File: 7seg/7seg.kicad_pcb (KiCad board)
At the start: 2 copper layers, 93.9 x 27.9 mm, 13 parts, among them J1 9pin_header, U1 LTS-4031JR, U2 LTS-4031JR, U3 LTS-4031JR, U4 LTS-4031JR, U5 LTS-4031JR, U6 LTS-4031JR, U7 LTS-4031JR, U8 LTS-4031JR

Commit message: more library changes
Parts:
- H1, H2, H3, H4: footprint MountingHole:MountingHole_2.2mm_M2_Pad -> footprints:MountingHole_2.2mm_M2_Pad
- J1: footprint SamacSys_Parts:HDRV9W63P0X254_1X9_2286X369X950P -> footprints:header
- U1, U2, U3, U4, U5, U6, U7, U8: footprint SamacSys_Parts:DIPS762W50P254L1290H725Q10N -> footprints:7seg

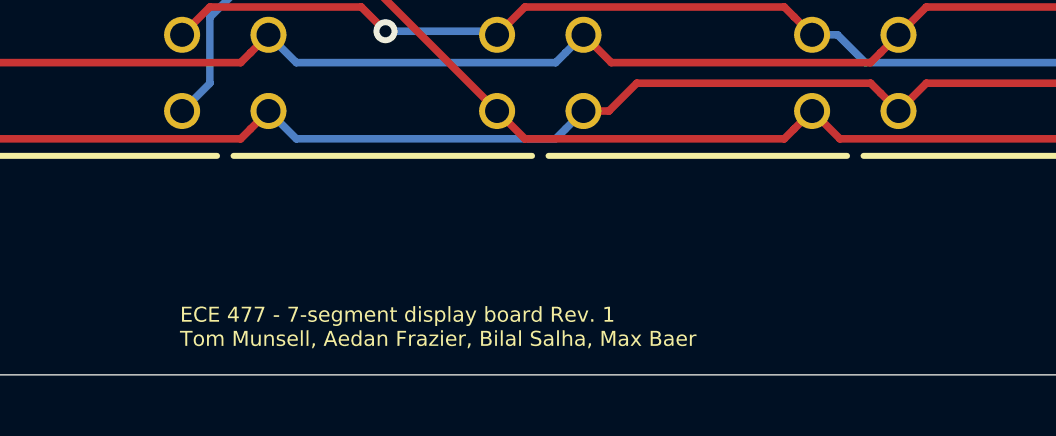
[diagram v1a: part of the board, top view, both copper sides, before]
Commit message: cleaned up directories, silkscreen
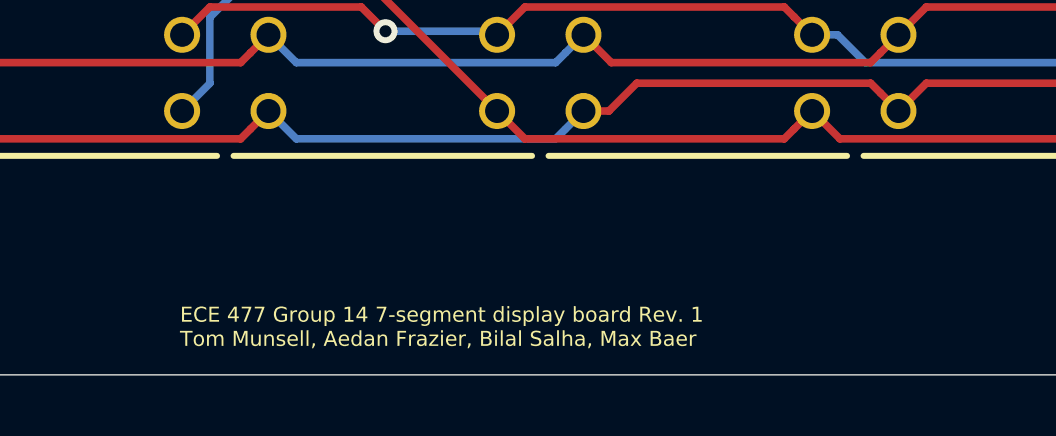
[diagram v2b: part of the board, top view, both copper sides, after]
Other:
- board text added: "ECE 477 Group 14 7-segment display board Rev. 1 Tom Munsell, Aedan Frazier, Bilal Salha, Max Baer"
- board text removed: "ECE 477 - 7-segment display board Rev. 1 Tom Munsell, Aedan Frazier, Bilal Salha, Max Baer"
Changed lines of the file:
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@@
       (net 7 "Net-(J1-Pad3)"))
   )
-  (gr_text "ECE 477 - 7-segment display board Rev. 1\nTom Munsell, Aedan Frazier, Bilal Salha, Max Baer" (at 82.55 92.3544) (layer F.SilkS)
+  (gr_text "ECE 477 Group 14 7-segment display board Rev. 1\nTom Munsell, Aedan Frazier, Bilal Salha, Max Baer" (at 82.55 92.3544) (layer F.SilkS)
     (effects (font (size 0.5 0.5) (thickness 0.125)) (justify left))
   )

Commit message: Added reset button, fixed 7seg pin order
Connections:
- net Net-(J1-Pad7) renamed /DIG6
- J1 pad 1: Net-(J1-Pad1) -> /DIG3
- J1 pad 2: Net-(J1-Pad2) -> /DIG2
- J1 pad 3: Net-(J1-Pad3) -> /DIG1
- J1 pad 4: Net-(J1-Pad4) -> /DIG0
- J1 pad 5: Net-(J1-Pad5) -> /a
- J1 pad 6: Net-(J1-Pad6) -> /DIG7
- J1 pad 8: Net-(J1-Pad8) -> /DIG5
- J1 pad 9: Net-(J1-Pad9) -> /DIG4
- U1 pad 1: Net-(J1-Pad3) -> /DIG2
- U1 pad 10: Net-(J1-Pad9) -> /a
- U1 pad 2: Net-(J1-Pad4) -> /DIG3
- U1 pad 3: Net-(J1-Pad1) -> /DIG0
- U1 pad 4: Net-(J1-Pad5) -> /DIG4
- U1 pad 5: Net-(J1-Pad6) -> /DIG5
- U1 pad 6: Net-(J1-Pad2) -> /DIG1
- U1 pad 8: Net-(J1-Pad1) -> /DIG0
- U1 pad 9: Net-(J1-Pad8) -> /DIG7
- U2 pad 1: Net-(J1-Pad3) -> /DIG2
- U2 pad 10: Net-(J1-Pad9) -> /a
- U2 pad 2: Net-(J1-Pad4) -> /DIG3
- U2 pad 3: Net-(J1-Pad2) -> /DIG1
- U2 pad 4: Net-(J1-Pad5) -> /DIG4
- U2 pad 5: Net-(J1-Pad6) -> /DIG5
- U2 pad 6: Net-(J1-Pad1) -> /DIG0
- U2 pad 8: Net-(J1-Pad2) -> /DIG1
- U2 pad 9: Net-(J1-Pad8) -> /DIG7
- U3 pad 1: Net-(J1-Pad2) -> /DIG1
- U3 pad 10: Net-(J1-Pad9) -> /a
- U3 pad 2: Net-(J1-Pad4) -> /DIG3
- U3 pad 3: Net-(J1-Pad3) -> /DIG2
- U3 pad 4: Net-(J1-Pad5) -> /DIG4
- U3 pad 5: Net-(J1-Pad6) -> /DIG5
- U3 pad 6: Net-(J1-Pad1) -> /DIG0
- U3 pad 8: Net-(J1-Pad3) -> /DIG2
- U3 pad 9: Net-(J1-Pad8) -> /DIG7
- U4 pad 1: Net-(J1-Pad2) -> /DIG1
- U4 pad 10: Net-(J1-Pad9) -> /a
- U4 pad 2: Net-(J1-Pad3) -> /DIG2
- U4 pad 3: Net-(J1-Pad4) -> /DIG3
- U4 pad 4: Net-(J1-Pad5) -> /DIG4
- U4 pad 5: Net-(J1-Pad6) -> /DIG5
- U4 pad 6: Net-(J1-Pad1) -> /DIG0
- U4 pad 8: Net-(J1-Pad4) -> /DIG3
- U4 pad 9: Net-(J1-Pad8) -> /DIG7
- U5 pad 1: Net-(J1-Pad2) -> /DIG1
- U5 pad 10: Net-(J1-Pad9) -> /a
- U5 pad 2: Net-(J1-Pad3) -> /DIG2
- U5 pad 3: Net-(J1-Pad5) -> /DIG4
- U5 pad 4: Net-(J1-Pad4) -> /DIG3
- U5 pad 5: Net-(J1-Pad6) -> /DIG5
- U5 pad 6: Net-(J1-Pad1) -> /DIG0
- U5 pad 8: Net-(J1-Pad5) -> /DIG4
- U5 pad 9: Net-(J1-Pad8) -> /DIG7
- U6 pad 1: Net-(J1-Pad2) -> /DIG1
- U6 pad 10: Net-(J1-Pad9) -> /a
- U6 pad 2: Net-(J1-Pad3) -> /DIG2
- U6 pad 3: Net-(J1-Pad6) -> /DIG5
- U6 pad 4: Net-(J1-Pad4) -> /DIG3
- U6 pad 5: Net-(J1-Pad5) -> /DIG4
- U6 pad 6: Net-(J1-Pad1) -> /DIG0
- U6 pad 8: Net-(J1-Pad6) -> /DIG5
- U6 pad 9: Net-(J1-Pad8) -> /DIG7
- U7 pad 1: Net-(J1-Pad2) -> /DIG1
- U7 pad 10: Net-(J1-Pad9) -> /a
- U7 pad 2: Net-(J1-Pad3) -> /DIG2
- U7 pad 4: Net-(J1-Pad4) -> /DIG3
- U7 pad 5: Net-(J1-Pad5) -> /DIG4
- U7 pad 6: Net-(J1-Pad1) -> /DIG0
- U7 pad 7: Net-(J1-Pad6) -> /DIG5
- U7 pad 9: Net-(J1-Pad8) -> /DIG7
- U8 pad 1: Net-(J1-Pad2) -> /DIG1
- U8 pad 10: Net-(J1-Pad9) -> /a
- U8 pad 2: Net-(J1-Pad3) -> /DIG2
- U8 pad 3: Net-(J1-Pad8) -> /DIG7
- U8 pad 4: Net-(J1-Pad4) -> /DIG3
- U8 pad 5: Net-(J1-Pad5) -> /DIG4
- U8 pad 6: Net-(J1-Pad1) -> /DIG0
- U8 pad 7: Net-(J1-Pad6) -> /DIG5
- U8 pad 8: Net-(J1-Pad8) -> /DIG7
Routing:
- net /DIG0: track 0.00 -> 134.6 mm
- net Net-(J1-Pad1): track 126.6 -> 0.00 mm
- net Net-(J1-Pad6): track 107.4 -> 0.00 mm
- net /DIG4: track 0.00 -> 103.4 mm
- net /DIG5: track 0.00 -> 103.1 mm
- net /DIG3: track 0.00 -> 98.3 mm
- net Net-(J1-Pad4): track 97.6 -> 0.00 mm
- net Net-(J1-Pad8): track 97.3 -> 0.00 mm
- net Net-(J1-Pad5): track 94.6 -> 0.00 mm
- net /DIG7: track 0.00 -> 94.1 mm
- net Net-(J1-Pad3): track 93.1 -> 0.00 mm
- net /DIG2: track 0.00 -> 92.1 mm
- net /DIG1: track 0.00 -> 88.0 mm
- net Net-(J1-Pad9): track 86.2 -> 0.00 mm
- net Net-(J1-Pad2): track 85.8 -> 0.00 mm
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
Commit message: gerbers
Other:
- rule pad_to_mask_clearance: 0.051 -> 0
